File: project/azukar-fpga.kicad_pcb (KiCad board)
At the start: 2 copper layers, 100 x 75 mm, 155 parts, among them J1 USB_C_Receptacle_USB2.0_16P, P1 Conector 2x10, P2 Conector 2x10, P3 Conector 2x10, P4 Conector 2x10, SW1 SW_Push, SW2 SW_Push, SW3 SW_Push, SW4 SW_Push, SW5 SW_Push, SW6 SW_Push, SW7 SW_Push, SW8 SW_Push, U1 LD1117S33CTR, U2 LD1117S12CTR, U3 USBLC6-2SC6, U4 FT2232HL, U5 M93C66, U6 ICE40HX4K-TQ144, U7 W25X40CLSN, Y1 ECS-3225MV-120-CN-TR, Y2 ECS-3225MVQ-1000-CN-TR

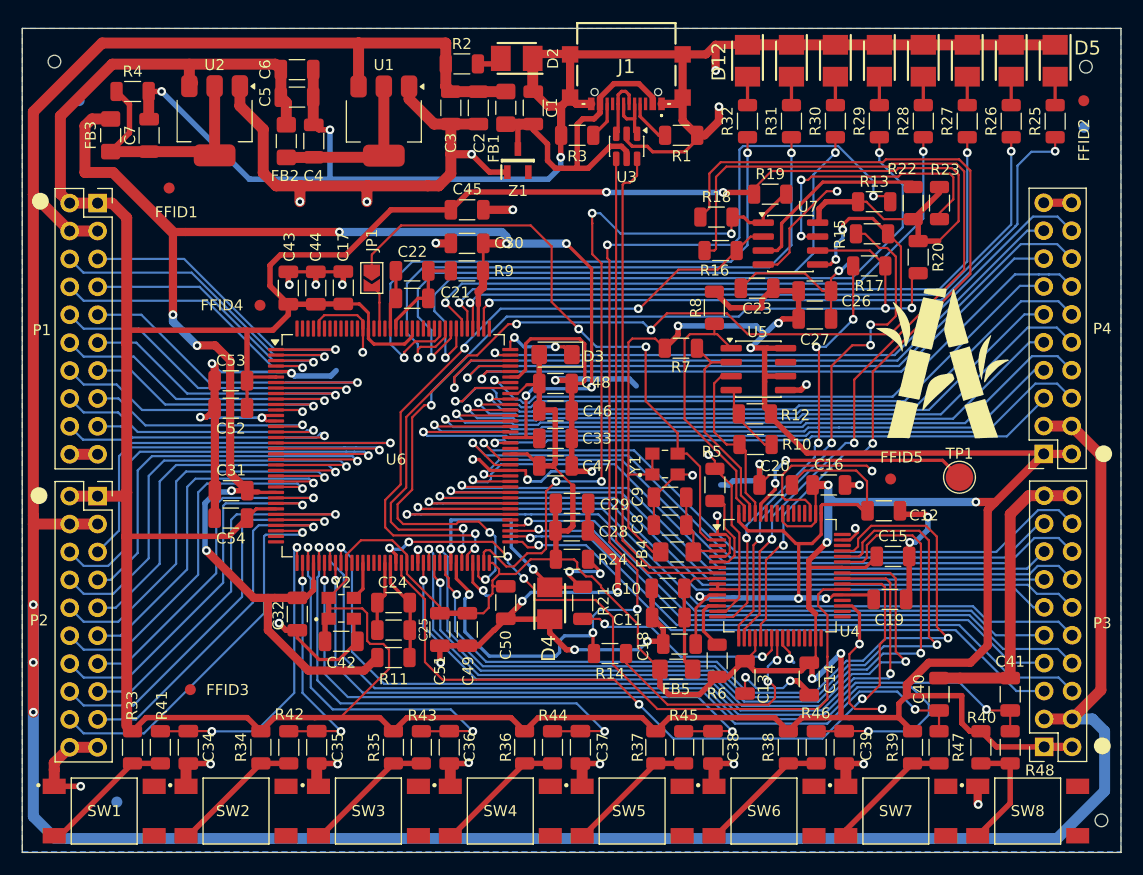
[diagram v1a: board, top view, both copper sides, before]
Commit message: Revision de traza de 3V3 que pasaba por debajo del cristal de 100, movido capacitor de 100 nF cerca del cristal de 12.
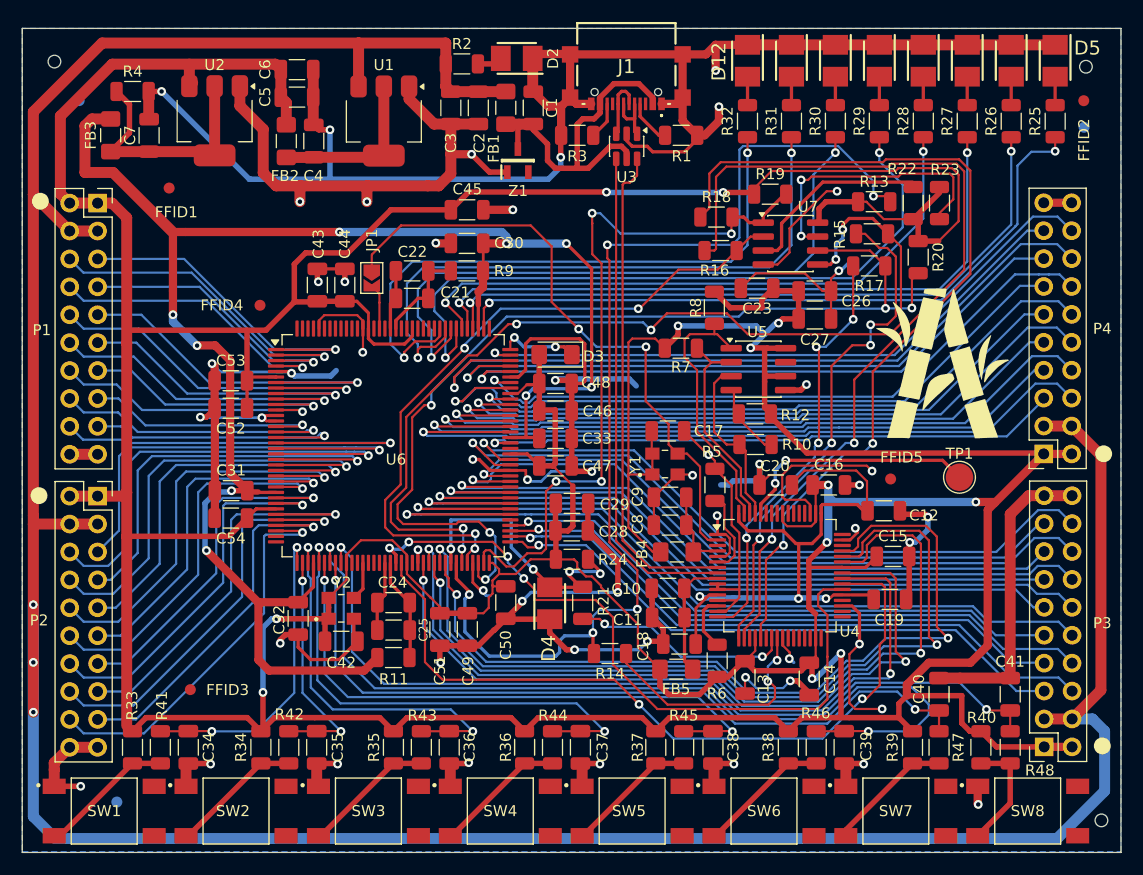
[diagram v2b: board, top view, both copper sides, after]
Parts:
- moved C17 32.3 mm to (178.8, 106.6), turned to 0 degrees
- moved C43 2.66 mm to (146.9, 93.4)
- moved C44 2.66 mm to (149.4, 93.4)
- moved C32 0.40 mm to (145.1, 123.7)
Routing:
- net +1V2: track 158.8 -> 161.0 mm
- net +3V3: track 658.6 -> 656.5 mm, vias 10 -> 12
- net GND: track 559.2 -> 558.8 mm, vias 55 -> 54

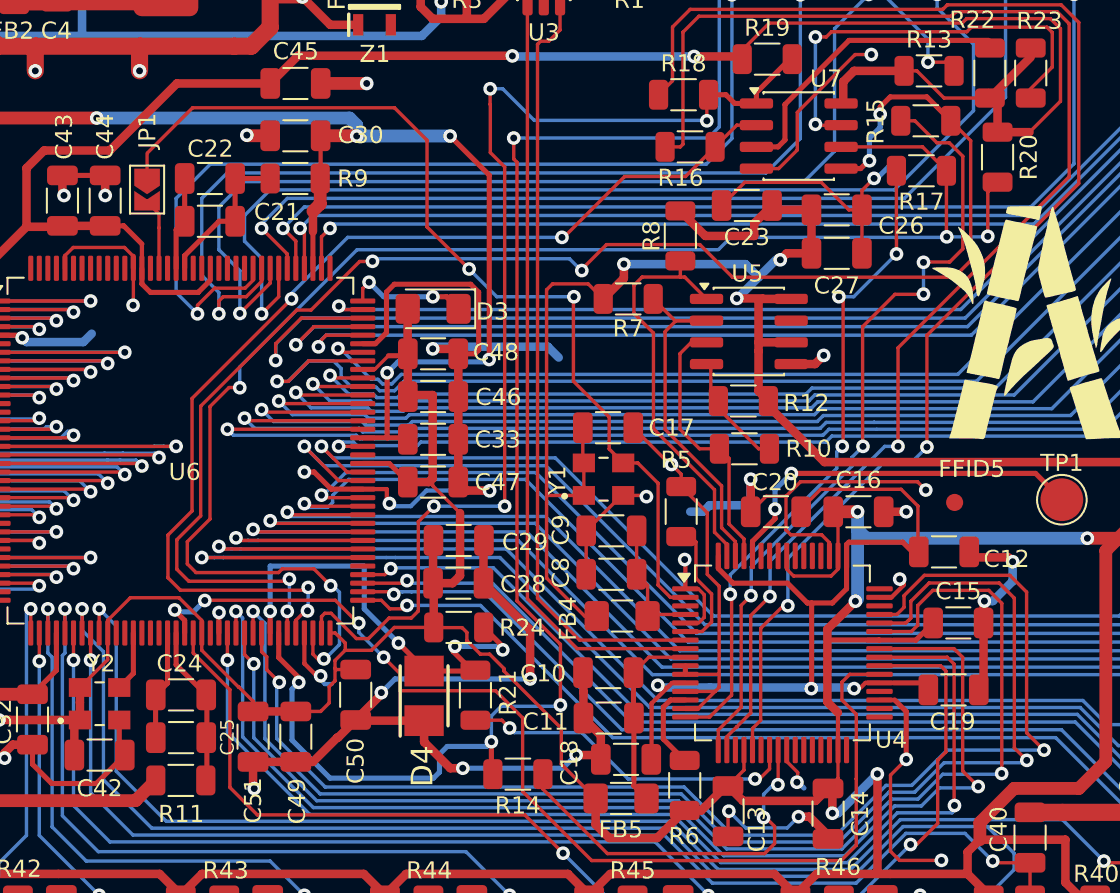
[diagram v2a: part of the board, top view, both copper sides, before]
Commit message: Eliminar mensaje de error - Issue #8. Mejora en algunas trazas del PCB, eliminacion de algunas vias ordenando mejor los componentes.
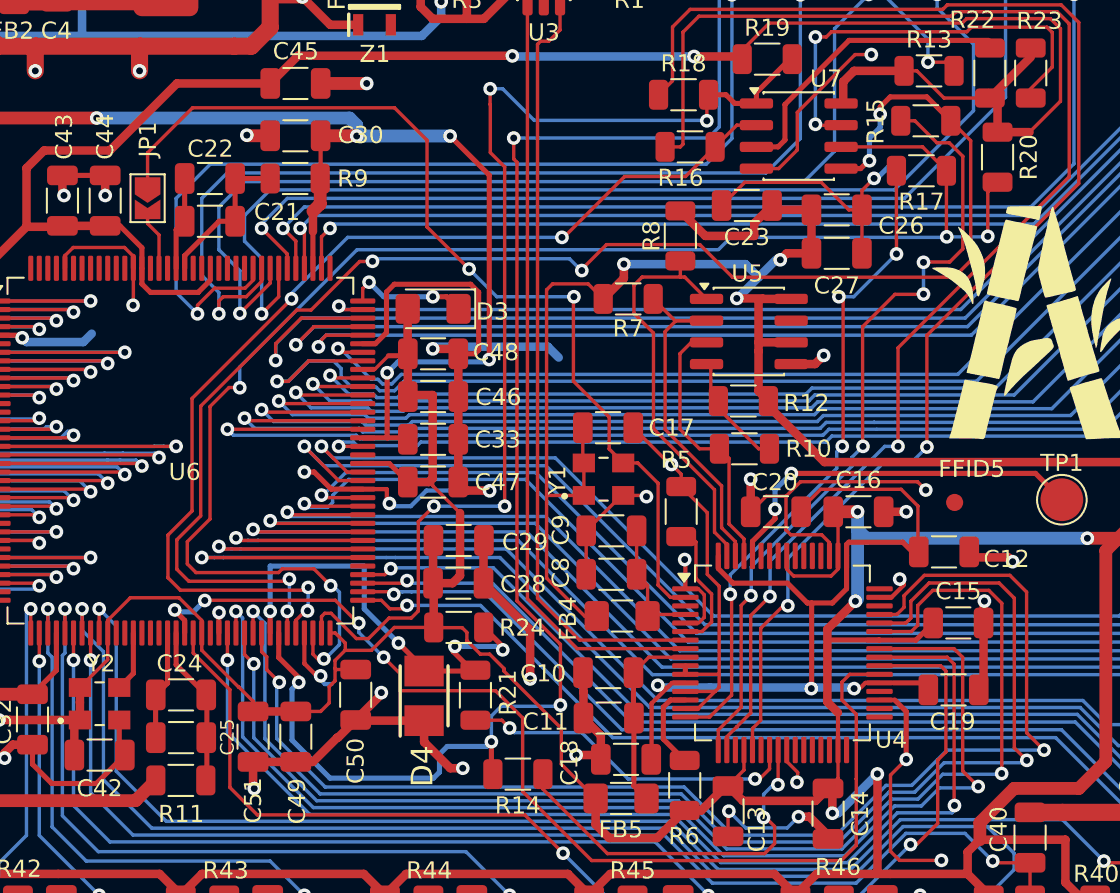
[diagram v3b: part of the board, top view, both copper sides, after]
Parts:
- moved JP1 0.51 mm to (151.8, 93.2)
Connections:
- net /Fuente de Alimentación/D+ renamed /Power Supply/D+
- net /Fuente de Alimentación/D- renamed /Power Supply/D-
- Z1 pad 2: unconnected-(Z1-NC-Pad2) -> (no net)
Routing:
- net GND: track 558.8 -> 534.1 mm
- net +3V3: track 656.5 -> 655.7 mm
- net /Perifericos/12MHz_CLK: track 56.3 -> 56.8 mm
- net Net-(JP1-B): track 4.17 -> 3.65 mm

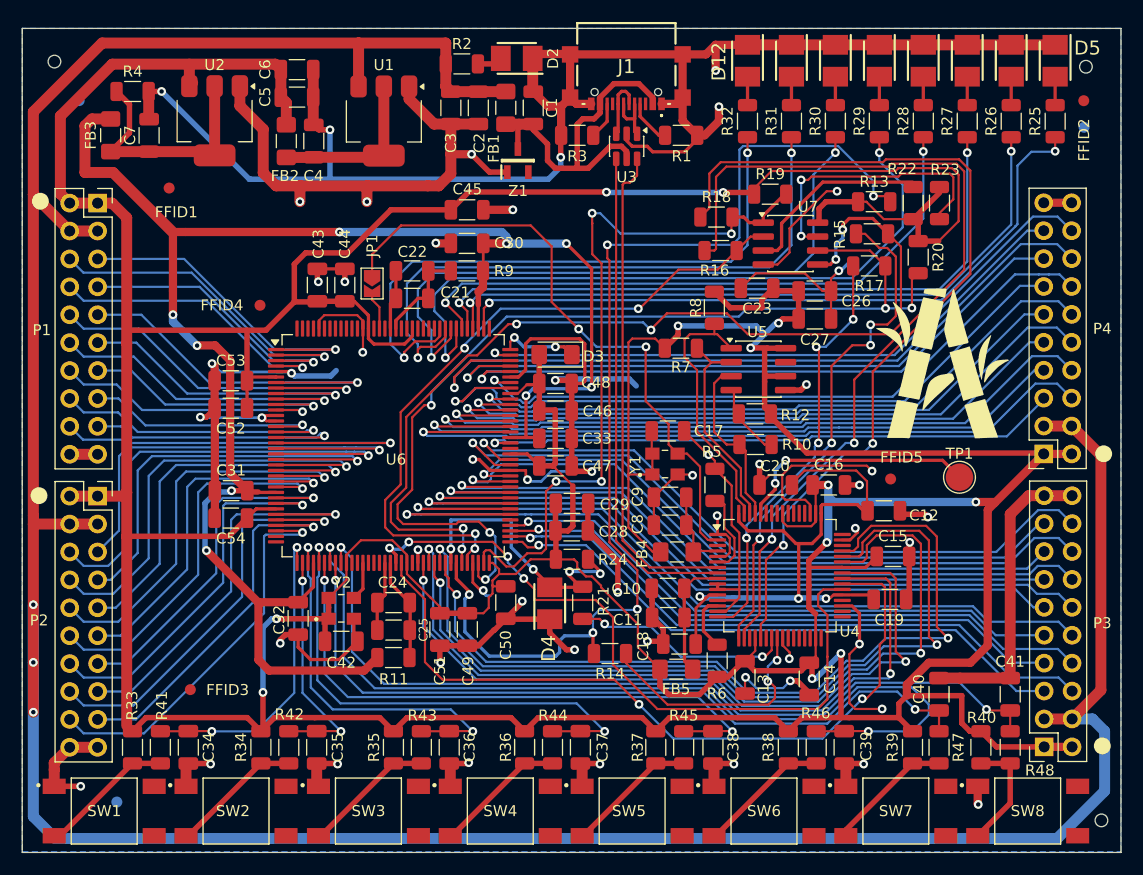
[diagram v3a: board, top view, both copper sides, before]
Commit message: Eliminar mensaje de error - Issue #8. Mejora en algunas trazas del PCB, eliminacion de algunas vias ordenando mejor los componentes.
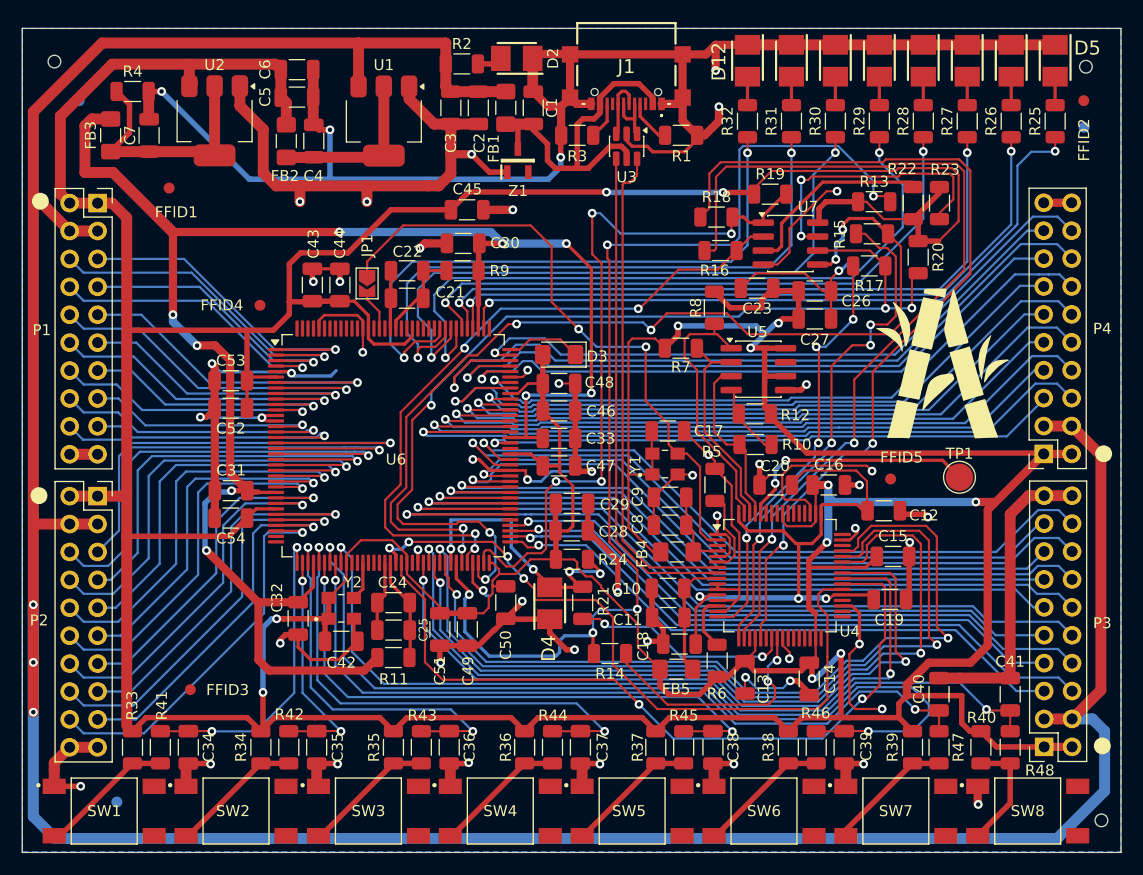
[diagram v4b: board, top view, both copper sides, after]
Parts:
- moved C43 0.45 mm to (146.4, 93.4)
- moved C44 0.45 mm to (148.9, 93.4)
- moved C21 0.45 mm to (155.0, 94.6)
- moved C22 0.45 mm to (155.0, 92.1)
- moved JP1 0.45 mm to (151.4, 93.2)
- moved R9 0.40 mm to (160.1, 92.1)
- moved C30 0.36 mm to (160.1, 89.6)
- moved C33 0.32 mm to (168.9, 107.3)
- moved C46 0.32 mm to (168.9, 104.8)
- moved C47 0.32 mm to (168.9, 109.8)
- moved C48 0.32 mm to (168.9, 102.3)
- moved D3 0.32 mm to (168.9, 99.7)
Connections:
- Z1 pad 2: (no net) -> unconnected-(Z1-NC-Pad2)
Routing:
- net GND: track 534.1 -> 515.2 mm, vias 54 -> 55
- net Net-(P4-IO13): track 66.8 -> 68.0 mm
- net Net-(P4-IO14): track 59.8 -> 61.0 mm
- net Net-(P2-IO10): track 34.9 -> 33.9 mm
- net Net-(P4-IO12): track 64.9 -> 66.0 mm
- net Net-(P2-IO9): track 33.0 -> 32.1 mm
- net Net-(P4-IO11): track 58.8 -> 59.6 mm
- net Net-(D3-K): track 7.13 -> 6.88 mm, vias 2 -> 0

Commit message: Mejorado el ruteo, eliminadas algunas vias, anillo de 3V3 cerrado
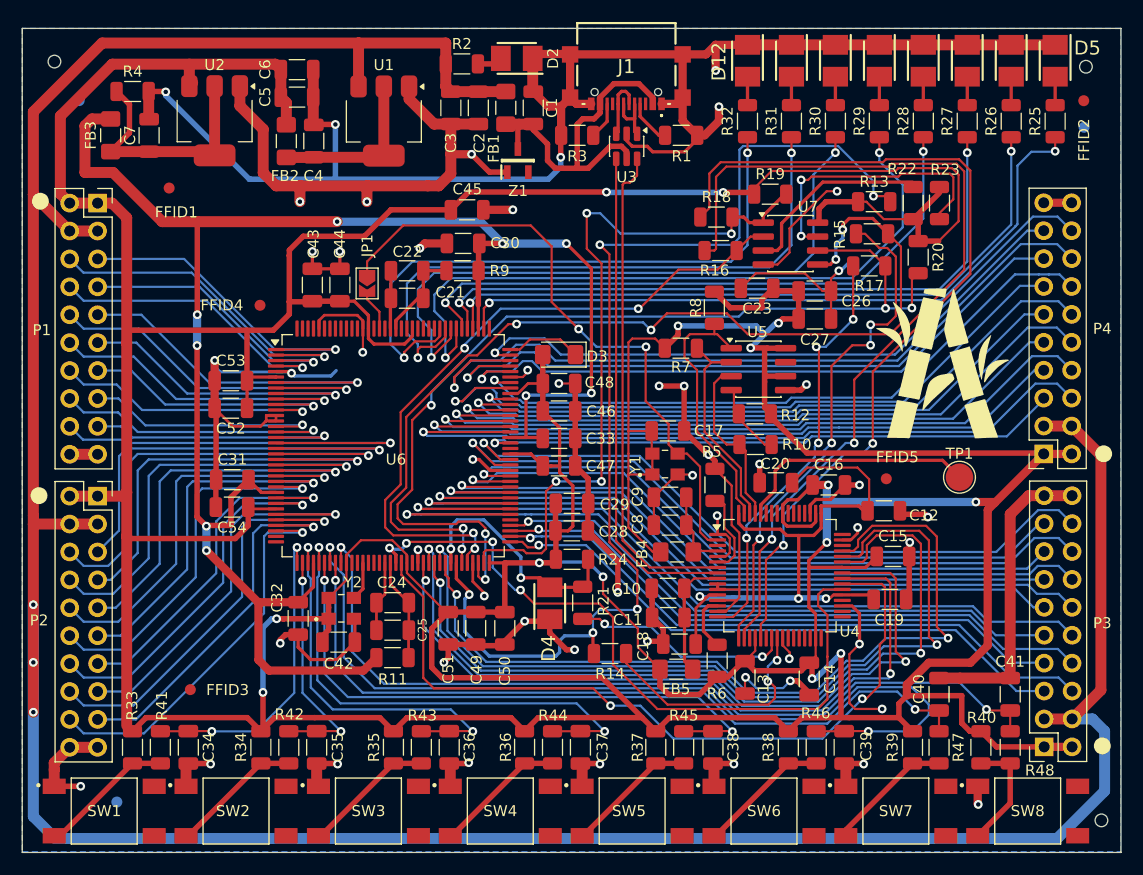
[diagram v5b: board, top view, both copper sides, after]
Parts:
- moved C50 2.35 mm to (163.9, 124.6)
- moved C31 1.00 mm to (139.1, 111.1)
- moved C54 1.00 mm to (139.1, 113.6)
- moved C49 0.77 mm to (161.3, 124.6)
- moved C51 0.77 mm to (158.8, 124.6)
- moved FFID5 0.39 mm to (198.6, 111.0)
- moved C42 0.25 mm to (148.8, 125.9)
- moved C20 0.20 mm to (188.6, 111.3)
- moved R11 0.08 mm to (153.7, 127.3)
- moved C24 0.08 mm to (153.7, 122.3)
- moved C25 0.08 mm to (153.7, 124.8)
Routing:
- net +3V3: track 655.7 -> 690.4 mm, vias 12 -> 14
- net GND: track 515.2 -> 500.0 mm, vias 55 -> 52
- net Net-(D4-A): track 26.8 -> 22.3 mm, vias 4 -> 2
- net +1V2: track 161.3 -> 162.7 mm
- net Net-(U6E-~{CRESET}): track 100.0 -> 101.0 mm
- net /Perifericos/VUART_Tx: track 69.3 -> 70.3 mm
- net Net-(P3-IO11): track 61.1 -> 60.2 mm
- net Net-(U6E-IOB_107_SCK): track 90.8 -> 89.9 mm
- net /Perifericos/VUART_Rx: track 64.1 -> 64.7 mm
- net Net-(P3-IO12): track 61.9 -> 61.4 mm
- net Net-(U4-~{PWREN}): vias 2 -> 0

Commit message: pequeño rework a la pcb
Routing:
- net +3V3: track 690.4 -> 687.1 mm
- net GND: track 500.0 -> 502.0 mm
- net Net-(J1-D--PadA7): track 6.37 -> 5.02 mm
- net Net-(U6E-IOB_106_SDI): track 62.9 -> 63.7 mm
- net Net-(U7-~{HOLD}): track 24.7 -> 25.3 mm
